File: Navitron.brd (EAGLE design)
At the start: 70 x 70 mm, 78 parts, among them J2 DX07S016JA1R1500, Q1 ROHM_RUM002N02T2LROHM_RUM002N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, Q2 2.5A/30V, Q3 ROHM_RUM002N02T2LROHM_RUM002N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, Q4 ROHM_RUM002N02T2LROHM_RUM002N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, Q5 ROHM_RUM002N02T2LROHM_RUM002N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, T1 BC847, T2 BC847, U1 ESP32-WROOM-32, U2 9DoF IMU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

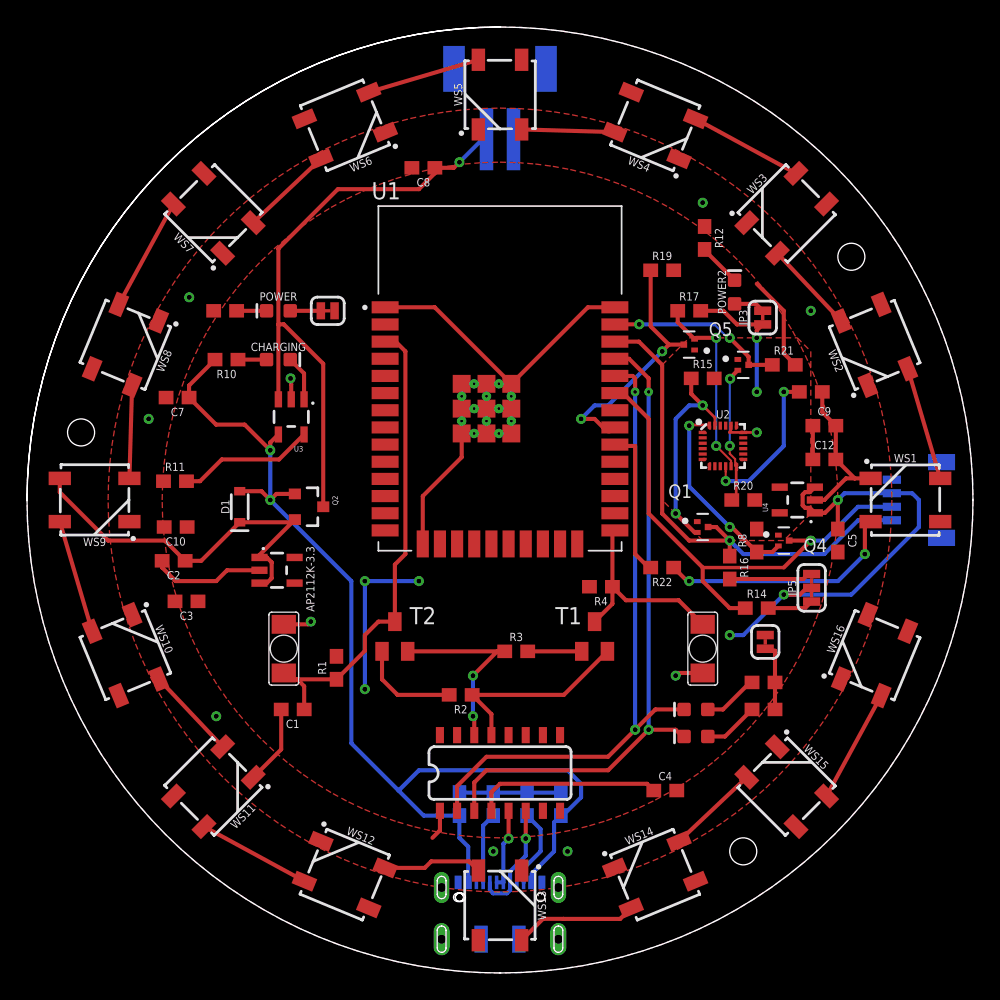
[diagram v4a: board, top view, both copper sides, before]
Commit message: Add Testingpoints
Added Testingpoints for:
- GND
- 3.3V
- 1.8V
- SDA
- SCL
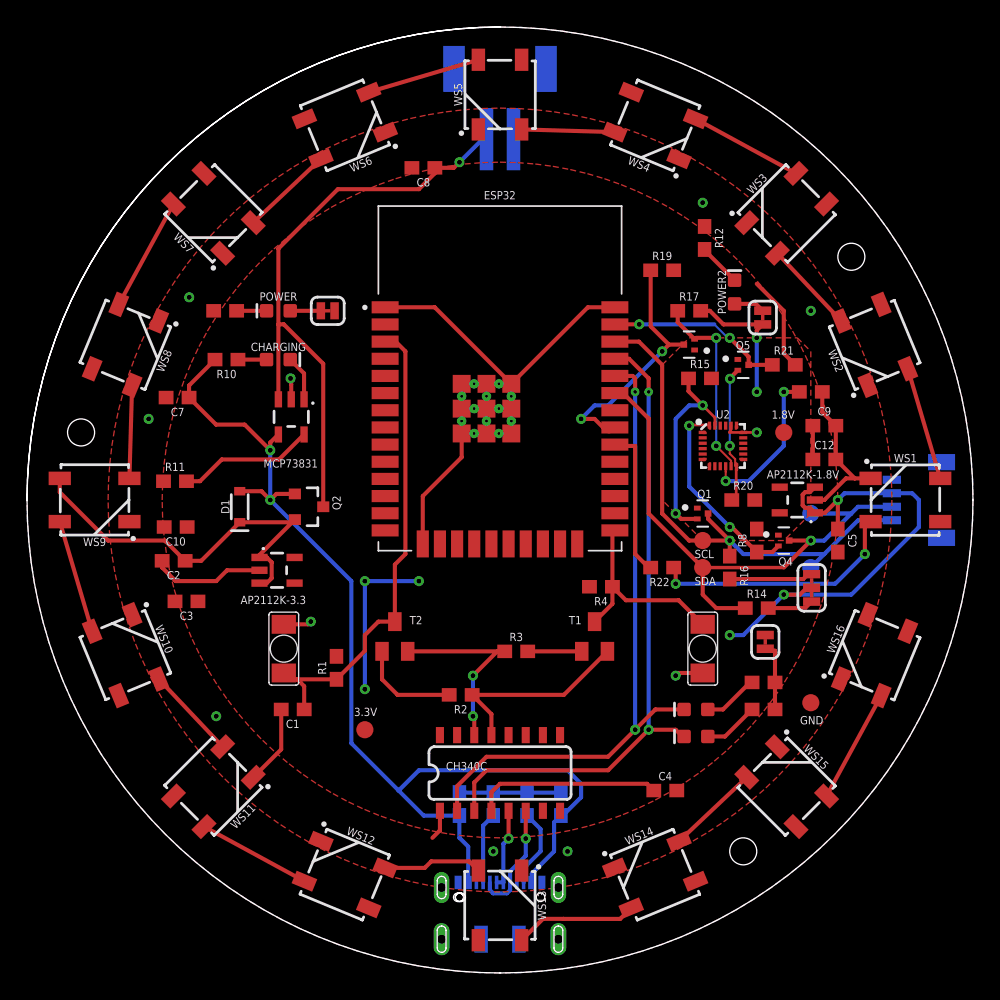
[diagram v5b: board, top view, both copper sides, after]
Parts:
- added 1.8V, 3.3V, GND, SCL, SCL1, SDA, SDA1: PTR1B1,27, testpad:B1,27
- moved Q1 1.00 mm to (50.0, 34.0)
- moved R15 0.20 mm to (49.8, 44.0)
- renumbered U1 to ESP32, U4 to AP2112K-1.8V
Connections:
- net 1.8V: now also 1.8V.TP
- net 3.3V: now also 3.3V.TP
- net GND: now also GND.TP
- net SCL: now also SCL.TP, SCL1.TP
- net SDA: now also SDA.TP, SDA1.TP
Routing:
- net SDA: track 38.4 -> 42.0 mm
- net SCL: track 38.2 -> 40.2 mm
- net DI_TO_WS: track 18.0 -> 18.7 mm
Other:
- board text added: "CH340C"
- board text added: "MCP73831"

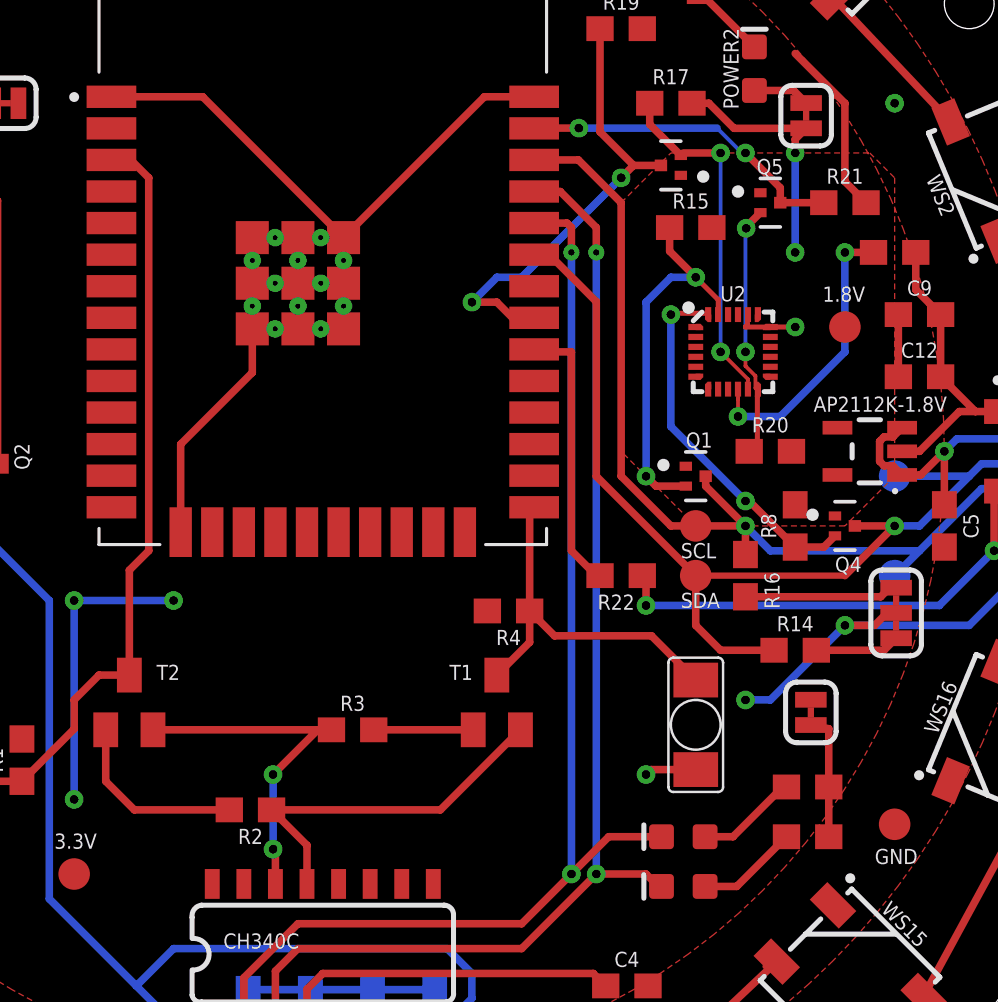
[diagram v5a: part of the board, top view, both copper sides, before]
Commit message: fix #1
- Fixed the heatsink, of the ICM-20948 briding the FSYNC and INT lines
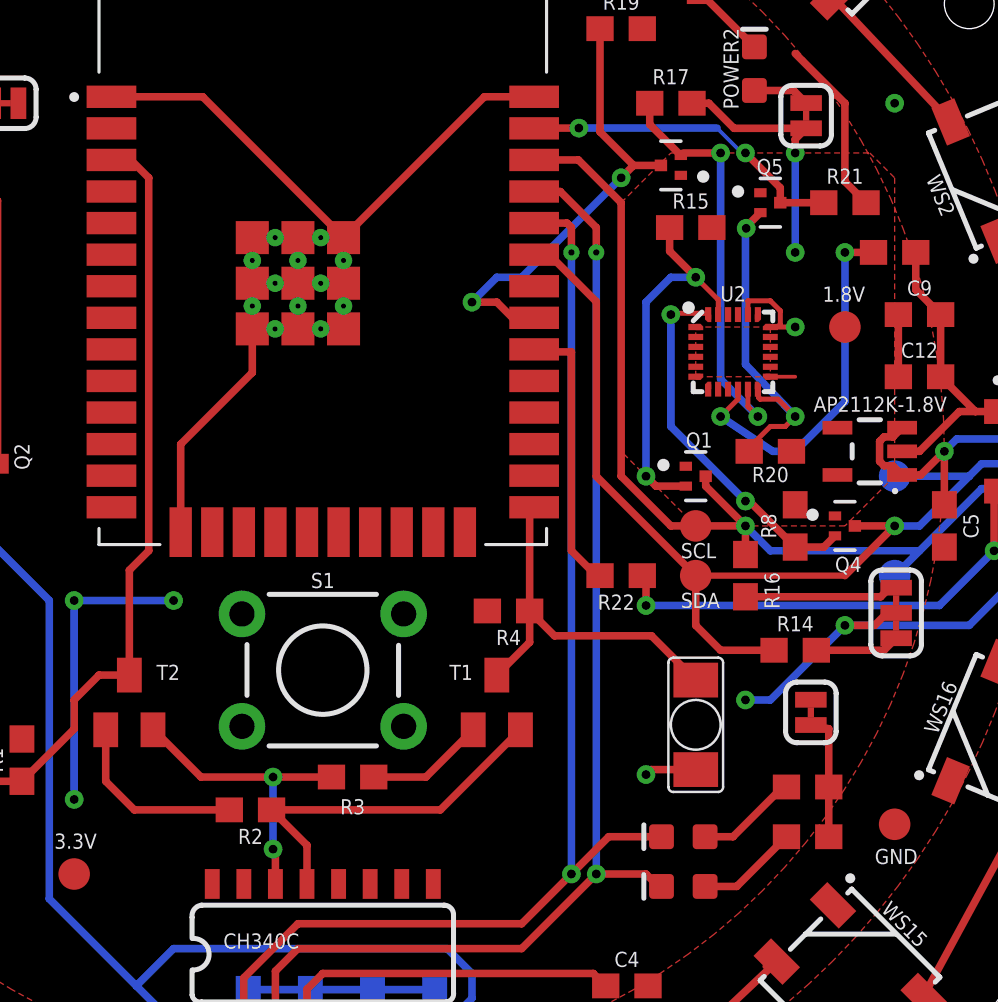
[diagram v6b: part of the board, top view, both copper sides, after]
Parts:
- added S1: MOMENTARY-SWITCH-SPST-PTH-6.0MM, SparkFun-Switches:TACTILE_SWITCH_PTH_6.0MM
- moved R3 1.90 mm to (36.2, 21.9)
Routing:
- net INT: track 10.0 -> 13.7 mm
- net REGOUT: track 11.6 -> 14.8 mm
- net FSYNC: track 14.2 -> 16.7 mm
- net !RTS: track 14.2 -> 12.3 mm
- net GND: track 75.9 -> 77.1 mm
- net 1.8V: track 13.1 -> 14.1 mm
- net TO_T1: track 4.00 -> 4.79 mm

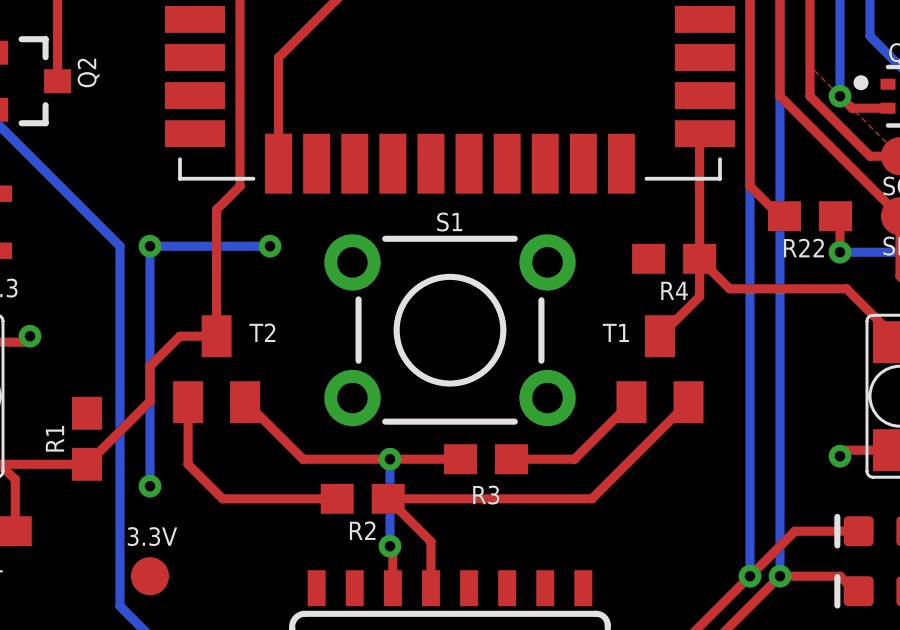
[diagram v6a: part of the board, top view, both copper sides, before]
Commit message: Remove Temporary Button
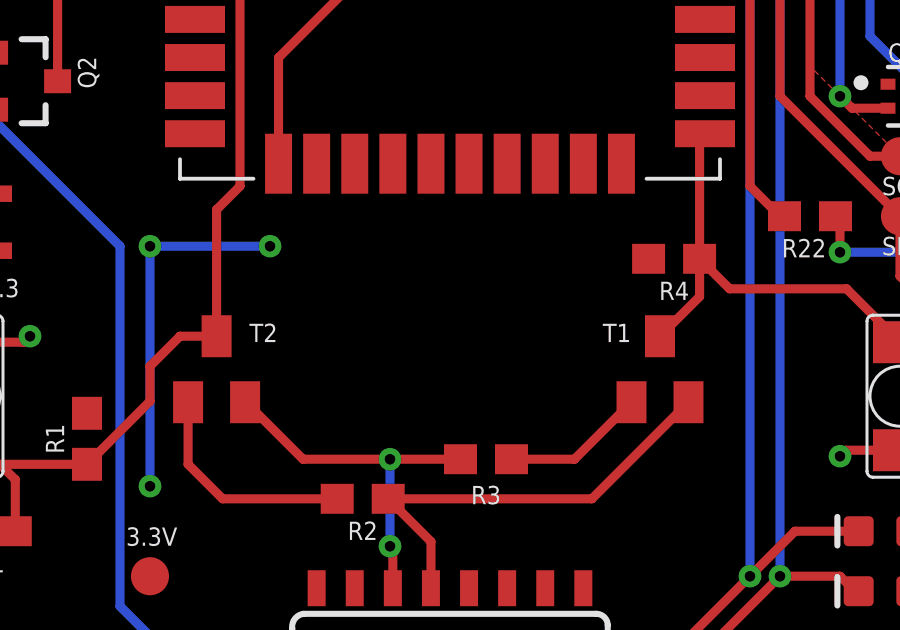
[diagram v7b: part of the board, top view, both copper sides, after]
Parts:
- removed S1: MOMENTARY-SWITCH-SPST-PTH-6.0MM, SparkFun-Switches:TACTILE_SWITCH_PTH_6.0MM
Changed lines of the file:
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@@
 <attribute name="VALUE" x="24.365" y="17.238" size="0.0254" layer="27"/>
-</element>
-<element name="S1" library="SparkFun-Switches" library_urn="urn:adsk.eagle:library:535" package="TACTILE_SWITCH_PTH_6.0MM" package3d_urn="urn:adsk.eagle:package:40163/1" value="MOMENTARY-SWITCH-SPST-PTH-6.0MM" x="35" y="26.2" smashed="yes">
-<attribute name="NAME" x="35" y="29.502" size="0.6096" layer="25" font="vector" ratio="20" align="bottom-center"/>
-<attribute name="PROD_ID" value=" SWCH-08441" x="35" y="26.2" size="1.778" layer="27" display="off"/>
-<attribute name="SF_SKU" value="COM-00097" x="35" y="26.2" size="1.778" layer="27" display="off"/>
-<attribute name="VALUE" x="35" y="23.025" size="0.6096" layer="27" font="vector" ratio="20" align="top-center"/>
 </element>
 </elements>

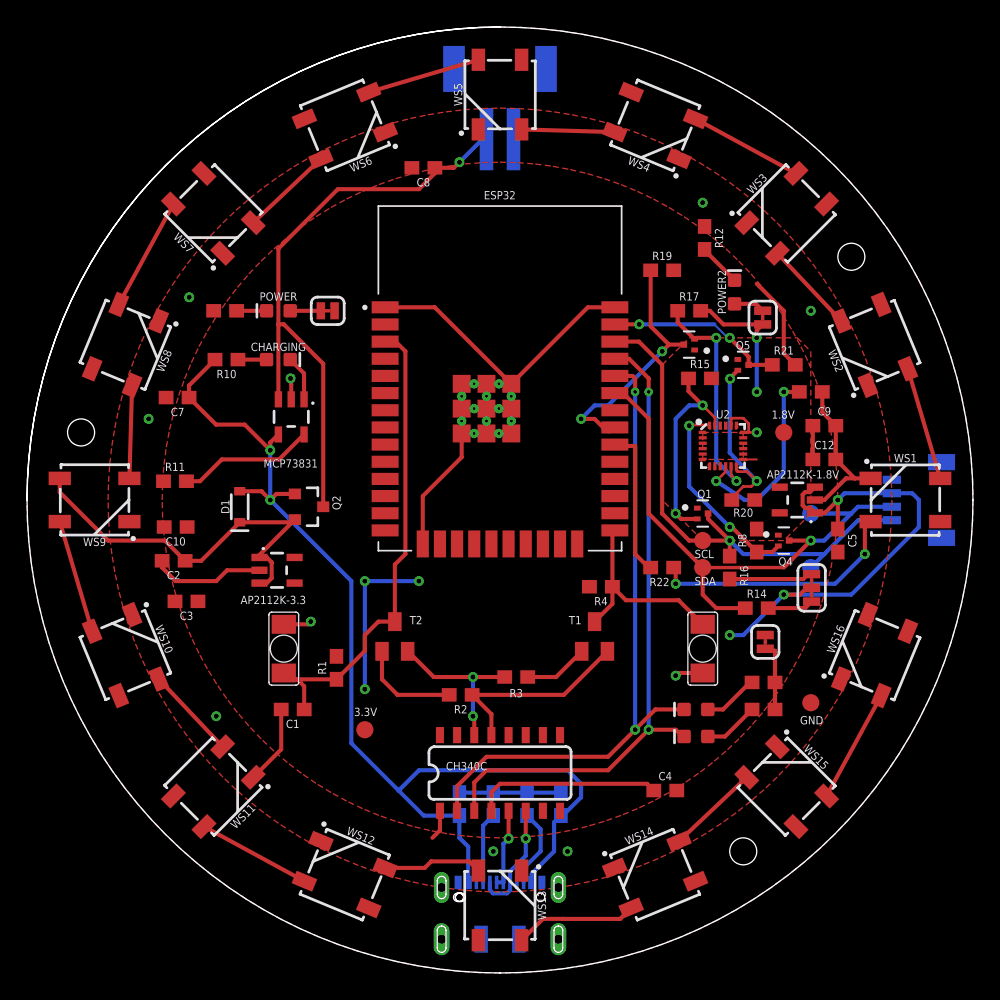
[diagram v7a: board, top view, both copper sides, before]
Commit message: Tented Vias + Some Changes
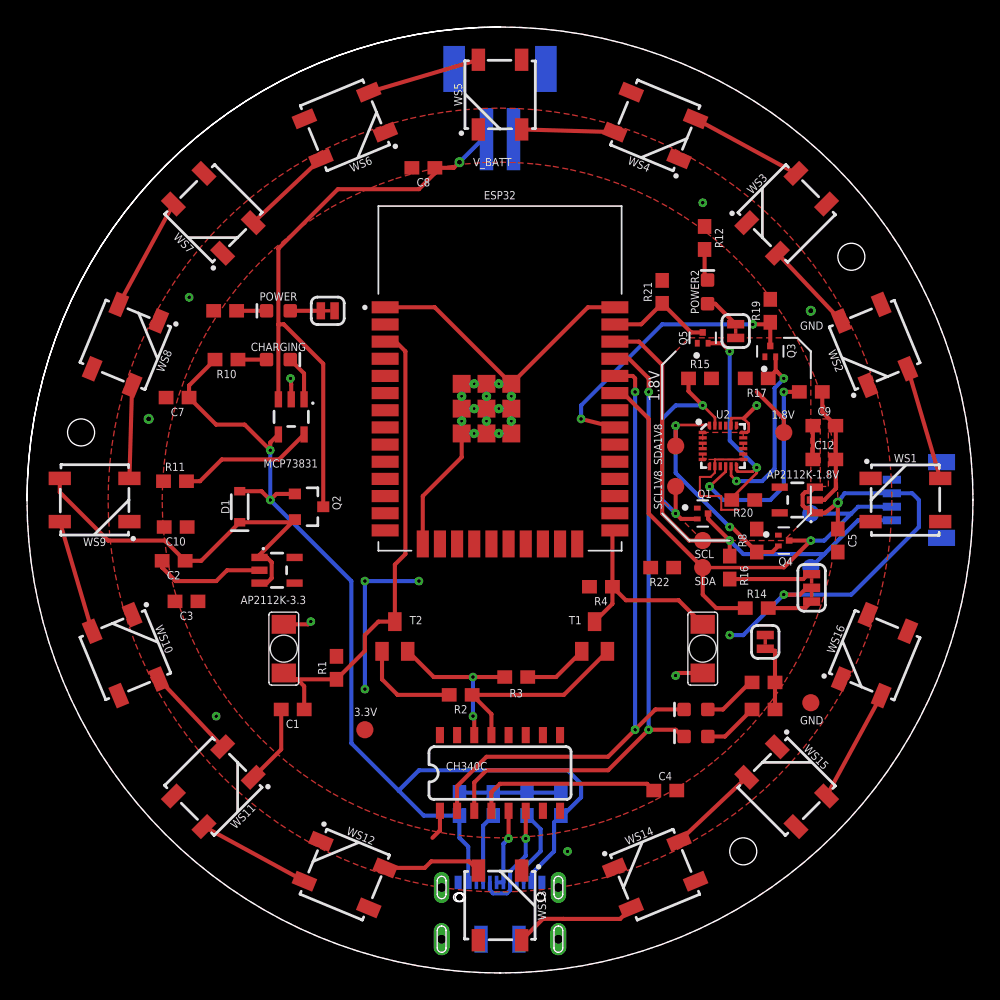
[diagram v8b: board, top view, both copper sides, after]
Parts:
- added SCL1V8, SDA1V8: PTR1B1,27, testpad:B1,27
- R9: value 1k -> 10MOHM-0603-1/10W-5%
- moved R21 10.5 mm to (47.0, 50.4), turned to 90 degrees
- moved R19 8.54 mm to (55.0, 49.0), turned to 90 degrees
- moved R17 7.07 mm to (54.0, 44.0), turned to 180 degrees
- moved Q3 6.02 mm to (55.0, 46.0), turned to 90 degrees
- moved Q5 3.61 mm to (50.0, 47.0), turned to 90 degrees
- moved JP3 2.24 mm to (52.4, 47.5)
- moved POWER2 2.00 mm to (50.4, 50.4)
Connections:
- net SCL1V8: now also SCL1V8.TP
- net SDA1V8: now also SDA1V8.TP
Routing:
- net DI_TO_WS: track 18.7 -> 0.00 mm, vias 2 -> 0
- net DI: track 11.1 -> 0.00 mm
- net 3.3V: track 55.2 -> 47.8 mm
- net INT_VIN: track 13.4 -> 8.04 mm, vias 2 -> 0
- net SCL1V8: track 15.5 -> 18.9 mm
- net FSYNC_VIN: track 18.8 -> 21.9 mm
- net SDA1V8: track 14.8 -> 17.8 mm
- net FSYNC: track 16.7 -> 14.1 mm
- net INT: track 13.7 -> 16.2 mm
- net 1.8V: track 14.1 -> 16.3 mm, vias 2 -> 0
- net GND: track 77.1 -> 75.0 mm, vias 11 -> 10
- net REGOUT: track 14.8 -> 16.5 mm
- net LED1.8_2: track 3.19 -> 2.35 mm
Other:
- board text added: "1.8V"
- board text added: "GND"
- board text added: "V_BATT"
